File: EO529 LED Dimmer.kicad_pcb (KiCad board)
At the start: 2 copper layers, 76.2 x 45.7 mm, 47 parts, among them J1 VBat, Q1 BC639, Q2 BC639, Q3 BC639, Q4 BC639, U1 NE556, U2 NE556

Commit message: Revision to circuit
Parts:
- removed D10: LED_RGBA, LED_THT:LED_BL-FL7680RGB
- removed D3, D4, D6, D7, D8, D9: 1N4148, Diode_THT:D_DO-35_SOD27_P7.62mm_Horizontal
- removed D5: White, LED_THT:LED_D10.0mm
- added R13: 10k, Resistor_THT:R_Axial_DIN0207_L6.3mm_D2.5mm_P7.62mm_Horizontal, F.Cu at (75.3, 81.7)
- added R14: 10k, Resistor_THT:R_Axial_DIN0207_L6.3mm_D2.5mm_P7.62mm_Horizontal, F.Cu at (82.9, 77.9)
- added R15: 100k, Resistor_THT:R_Axial_DIN0207_L6.3mm_D2.5mm_P7.62mm_Horizontal, F.Cu at (60.7, 38.9)
- added R16: 100k, Resistor_THT:R_Axial_DIN0207_L6.3mm_D2.5mm_P7.62mm_Horizontal, F.Cu at (76.9, 23.3)
- added R17: 1k, Resistor_THT:R_Axial_DIN0207_L6.3mm_D2.5mm_P7.62mm_Horizontal, F.Cu at (66.1, 31.4)
- added R18: 180, Resistor_THT:R_Axial_DIN0207_L6.3mm_D2.5mm_P7.62mm_Horizontal, F.Cu at (47.0, 51.1)
- added R19: 10k, Resistor_THT:R_Axial_DIN0207_L6.3mm_D2.5mm_P7.62mm_Horizontal, F.Cu at (61.3, 81.7)
- added R20: 10k, Resistor_THT:R_Axial_DIN0207_L6.3mm_D2.5mm_P7.62mm_Horizontal, F.Cu at (53.7, 77.9)
- added R21: 100k, Resistor_THT:R_Axial_DIN0207_L6.3mm_D2.5mm_P7.62mm_Horizontal, F.Cu at (39.2, 47.0)
- added R22: 100k, Resistor_THT:R_Axial_DIN0207_L6.3mm_D2.5mm_P7.62mm_Horizontal, F.Cu at (76.9, 19.3)
- added R23: 1k, Resistor_THT:R_Axial_DIN0207_L6.3mm_D2.5mm_P7.62mm_Horizontal, F.Cu at (39.2, 43.0)
- added R24: 220, Resistor_THT:R_Axial_DIN0207_L6.3mm_D2.5mm_P7.62mm_Horizontal, F.Cu at (49.9, 38.9)
- added U3: LM339, Package_DIP:DIP-14_W7.62mm_Socket, F.Cu at (33.4, 87.4)
- D1: value 1N4148 -> White; footprint Diode_THT:D_DO-35_SOD27_P7.62mm_Horizontal -> LED_THT:LED_D10.0mm
- D2: value 1N4148 -> LED_RGBA; footprint Diode_THT:D_DO-35_SOD27_P7.62mm_Horizontal -> LED_THT:LED_BL-FL7680RGB
- R1, R2, R7, R8: value 1k -> 10k
- R10, R3, R4, R9: value 1k -> 100k
- R12: value 1k -> 220
- R5: value 180 -> 1k
- R6: value 10k -> 150
- moved D2 71.5 mm to (88.3, 15.4), turned to 0 degrees
- moved H2 68.9 mm to (87.0, 46.4)
- moved H1 65.7 mm to (87.5, 40.5)
- moved R7 60.0 mm to (75.3, 85.5)
- moved RV2 51.8 mm to (49.3, 102.0), turned to 90 degrees
- moved RV3 48.9 mm to (43.6, 65.2), turned to 270 degrees
- moved C6 48.4 mm to (81.7, 74.0), turned to 90 degrees
- moved R8 47.3 mm to (82.9, 89.3), turned to 180 degrees
- moved Q1 46.7 mm to (80.0, 40.7), turned to 0 degrees
- moved R10 44.7 mm to (66.1, 23.3), turned to 0 degrees
- moved Q4 42.9 mm to (79.5, 46.5), turned to 0 degrees
- moved C3 42.5 mm to (76.6, 93.1), turned to 270 degrees
- moved RV1 39.8 mm to (37.8, 102.0), turned to 90 degrees
- moved C8 39.1 mm to (55.0, 74.0), turned to 90 degrees
- moved R4 37.9 mm to (66.1, 15.2)
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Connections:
- D1 pad 2: Net-(D1-Pad2) -> VCC
- D2 pad 1: Net-(D1-Pad2) -> Red
- D2 pad 2: Net-(D2-Pad2) -> Green
- R1 pad 1: Net-(Q1-Pad3) -> VCC
- R10 pad 1: Net-(Q2-Pad2) -> Net-(R10-Pad1)
- R10 pad 2: Net-(D5-Pad1) -> GND
- R11 pad 1: Net-(Q4-Pad2) -> Net-(Q2-Pad3)
- R11 pad 2: Green -> Net-(R11-Pad2)
- R12 pad 1: Net-(Q3-Pad2) -> Net-(Q2-Pad2)
- R12 pad 2: Blue -> Green
- R2 pad 1: Net-(Q2-Pad3) -> Net-(R1-Pad2)
- R2 pad 2: Net-(R2-Pad2) -> Net-(C2-Pad1)
- R3 pad 2: Net-(D1-Pad2) -> Net-(R3-Pad2)
- R4 pad 1: VCC -> Net-(R4-Pad1)
- R4 pad 2: Net-(D3-Pad2) -> GND
- R5 pad 1: Net-(Q1-Pad2) -> Net-(Q1-Pad3)
- R5 pad 2: Red -> Net-(R5-Pad2)
- R6 pad 1: Net-(Q3-Pad3) -> Net-(Q1-Pad2)
- R6 pad 2: Net-(R6-Pad2) -> Red
- R7 pad 1: Net-(Q4-Pad3) -> VCC
- R8 pad 1: VCC -> Net-(R7-Pad2)
- R8 pad 2: Net-(D6-Pad2) -> Net-(C4-Pad1)
- R9 pad 2: Net-(D8-Pad2) -> Net-(R9-Pad2)
- RV1 pad 1: Net-(D1-Pad1) -> Net-(R4-Pad1)
- RV1 pad 2: Net-(C3-Pad1) -> Net-(RV1-Pad2)
- RV1 pad 3: Net-(D2-Pad2) -> Net-(R3-Pad2)
- RV2 pad 1: Net-(D3-Pad1) -> Net-(R10-Pad1)
- RV2 pad 2: Net-(C4-Pad1) -> Net-(RV2-Pad2)
- RV2 pad 3: Net-(D4-Pad2) -> Net-(R9-Pad2)
- RV3 pad 2: Net-(C7-Pad1) -> Net-(RV3-Pad2)
- RV4 pad 2: Net-(C8-Pad1) -> Net-(RV4-Pad2)
- U1 pad 1: Net-(D1-Pad2) -> Net-(R1-Pad2)
- U1 pad 11: Net-(C2-Pad1) -> Net-(C3-Pad1)
- U1 pad 13: Net-(D3-Pad2) -> Net-(R7-Pad2)
- U1 pad 2: Net-(C3-Pad1) -> Net-(C2-Pad1)
- U1 pad 5: Net-(R1-Pad2) -> (no net)
- U1 pad 6: Net-(C3-Pad1) -> Net-(C2-Pad1)
- U1 pad 9: Net-(R2-Pad2) -> (no net)
- U2 pad 1: Net-(D6-Pad2) -> Net-(R13-Pad2)
- U2 pad 11: Net-(C6-Pad1) -> Net-(C7-Pad1)
- U2 pad 13: Net-(D8-Pad2) -> Net-(R19-Pad2)
- U2 pad 2: Net-(C7-Pad1) -> Net-(C6-Pad1)
- U2 pad 5: Net-(R6-Pad2) -> (no net)
- U2 pad 6: Net-(C7-Pad1) -> Net-(C6-Pad1)
- U2 pad 9: Net-(R7-Pad2) -> (no net)
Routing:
- net GND: track 210.0 -> 61.6 mm
- net Net-(C6-Pad1): track 3.91 -> 76.7 mm
- net Green: track 70.3 -> 0.00 mm
- net Red: track 65.9 -> 0.00 mm
- net VCC: track 119.5 -> 59.6 mm
- net Blue: track 44.4 -> 0.00 mm
- net Net-(C4-Pad1): track 39.2 -> 80.8 mm
- net Net-(C2-Pad1): track 3.91 -> 41.9 mm
- net Net-(C7-Pad1): track 40.2 -> 4.45 mm
- net Net-(C3-Pad1): track 37.2 -> 4.45 mm
- net Net-(D5-Pad1): track 32.6 -> 0.00 mm
- net Net-(D6-Pad2): track 24.0 -> 0.00 mm
- net Net-(D1-Pad2): track 23.6 -> 0.00 mm
- net Net-(D3-Pad2): track 23.2 -> 0.00 mm
- net Net-(D8-Pad2): track 22.6 -> 0.00 mm
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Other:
- board outline removed
- board text removed: "+ -"
- board text removed: "PWM LED Controller Board EO529 Part A"
- board text removed: "University of Brighton EEE V1.0 Aria Tso 21839447"

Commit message: Fixed broken files
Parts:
- added U4: LM393, Package_DIP:DIP-8_W7.62mm_Socket, F.Cu at (129.5, 90.8)
- R24: value 220 -> 150
- R6: value 150 -> 220
- U3: value LM339 -> LM393; footprint Package_DIP:DIP-14_W7.62mm_Socket -> Package_DIP:DIP-8_W7.62mm_Socket
- moved D1 109.1 mm to (110.5, 116.8), turned to 90 degrees
- moved R16 106.2 mm to (128.3, 116.2)
- moved R18 103.3 mm to (137.2, 101.6), turned to 270 degrees
- moved R11 102.2 mm to (133.3, 87.6), turned to 90 degrees
- moved R15 101.0 mm to (125.7, 116.2), turned to 180 degrees
- moved D2 100.0 mm to (97.8, 114.9)
- moved R12 98.0 mm to (137.2, 87.6), turned to 90 degrees
- moved R17 97.2 mm to (133.3, 101.6), turned to 270 degrees
- moved RV3 96.9 mm to (128.2, 112.2), turned to 90 degrees
- moved R22 92.5 mm to (73.7, 111.8), turned to 270 degrees
- moved H4 89.7 mm to (139.7, 119.4)
- moved R21 84.7 mm to (95.9, 109.9), turned to 180 degrees
- moved Q3 80.3 mm to (137.2, 97.2), turned to 180 degrees
- moved J1 78.3 mm to (88.9, 118.1), turned to 180 degrees
- moved RV2 78.1 mm to (123.2, 77.0), turned to 270 degrees
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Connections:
- R12 pad 2: Green -> Blue
- R24 pad 2: Blue -> Red
- R6 pad 2: Red -> Green
- U1 pad 5: (no net) -> Net-(U1-Pad5)
- U1 pad 9: (no net) -> Net-(U1-Pad9)
- U2 pad 5: (no net) -> Net-(U2-Pad5)
- U2 pad 9: (no net) -> Net-(U2-Pad9)
- U3 pad 1: Net-(R11-Pad2) -> Net-(R23-Pad2)
- U3 pad 2: Net-(R5-Pad2) -> Net-(C8-Pad1)
- U3 pad 3: VCC -> Net-(RV4-Pad2)
- U3 pad 4: Net-(C2-Pad1) -> GND
- U3 pad 6: Net-(C4-Pad1) -> Net-(C2-Pad1)
- U3 pad 7: Net-(RV2-Pad2) -> Net-(R5-Pad2)
- U3 pad 8: Net-(C6-Pad1) -> VCC
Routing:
- net GND: track 61.6 -> 285.7 mm
- net VCC: track 59.6 -> 194.7 mm
- net Blue: track 0.00 -> 75.9 mm
- net Green: track 0.00 -> 70.1 mm
- net Net-(C6-Pad1): track 76.7 -> 31.2 mm
- net Net-(C4-Pad1): track 80.8 -> 44.0 mm
- net Net-(D1-Pad1): track 0.00 -> 31.3 mm
- net Red: track 0.00 -> 27.5 mm
- net Net-(R17-Pad2): track 0.00 -> 17.6 mm
- net Net-(R23-Pad2): track 0.00 -> 14.0 mm
- net Net-(Q1-Pad3): track 0.00 -> 13.4 mm
- net Net-(R11-Pad2): track 0.00 -> 12.4 mm
- net Net-(Q2-Pad3): track 0.00 -> 12.2 mm
- net Net-(R22-Pad1): track 0.00 -> 12.0 mm
- net Net-(R9-Pad2): track 0.00 -> 11.7 mm
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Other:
- board outline added: 77.5 x 52.7 mm
- board text added: "- +"

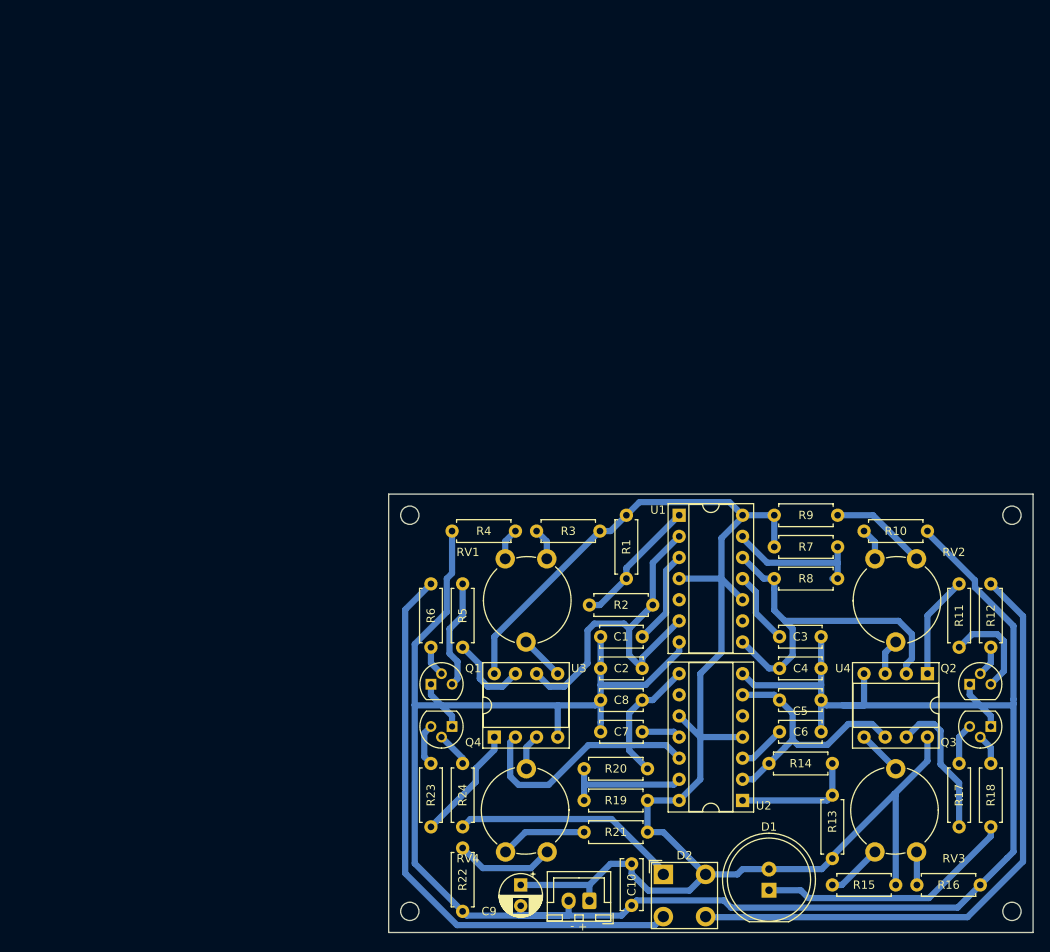
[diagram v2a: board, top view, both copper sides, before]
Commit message: Revert "Fixed broken files"
This reverts commit e50aa6ede737ee02b3ead64743985b0a59545fc6.
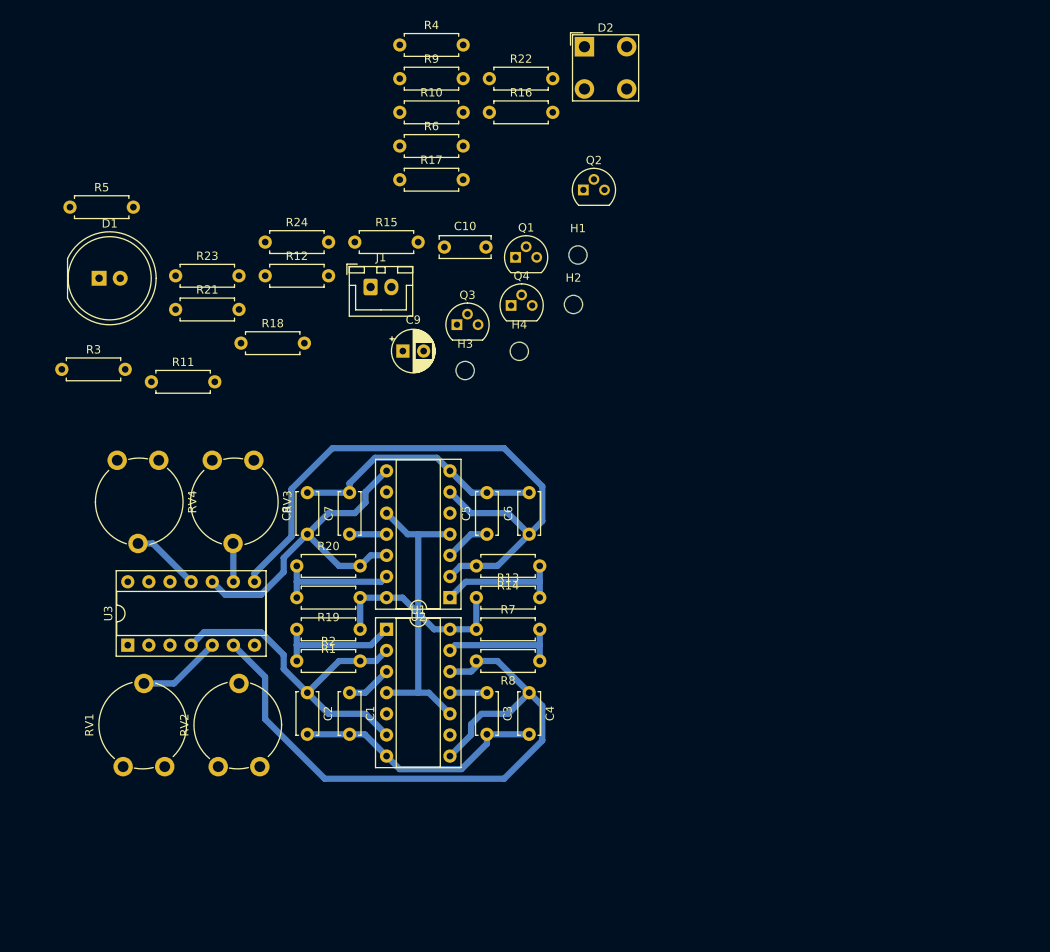
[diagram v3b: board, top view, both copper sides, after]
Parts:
- removed U4: LM393, Package_DIP:DIP-8_W7.62mm_Socket
- R24: value 150 -> 220
- R6: value 220 -> 150
- U3: value LM393 -> LM339; footprint Package_DIP:DIP-8_W7.62mm_Socket -> Package_DIP:DIP-14_W7.62mm_Socket
- moved D1 109.1 mm to (30.0, 43.3), turned to 0 degrees
- moved R16 106.2 mm to (76.9, 23.3)
- moved R18 103.3 mm to (47.0, 51.1), turned to 0 degrees
- moved R11 102.2 mm to (36.2, 55.7), turned to 0 degrees
- moved R15 101.0 mm to (60.7, 38.9), turned to 0 degrees
- moved D2 100.0 mm to (88.3, 15.4)
- moved R12 98.0 mm to (49.9, 43.0), turned to 0 degrees
- moved R17 97.2 mm to (66.1, 31.4), turned to 0 degrees
- moved RV3 96.9 mm to (43.6, 65.2), turned to 270 degrees
- moved R22 92.5 mm to (76.9, 19.3), turned to 0 degrees
- moved H4 89.7 mm to (80.5, 52.0)
- moved R21 84.7 mm to (39.2, 47.0), turned to 0 degrees
- moved Q3 80.3 mm to (73.0, 48.8), turned to 0 degrees
- moved J1 78.3 mm to (62.6, 44.3), turned to 0 degrees
- moved RV2 78.1 mm to (49.3, 102.0), turned to 90 degrees
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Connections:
- R12 pad 2: Blue -> Green
- R24 pad 2: Red -> Blue
- R6 pad 2: Green -> Red
- U1 pad 5: Net-(U1-Pad5) -> (no net)
- U1 pad 9: Net-(U1-Pad9) -> (no net)
- U2 pad 5: Net-(U2-Pad5) -> (no net)
- U2 pad 9: Net-(U2-Pad9) -> (no net)
- U3 pad 1: Net-(R23-Pad2) -> Net-(R11-Pad2)
- U3 pad 2: Net-(C8-Pad1) -> Net-(R5-Pad2)
- U3 pad 3: Net-(RV4-Pad2) -> VCC
- U3 pad 4: GND -> Net-(C2-Pad1)
- U3 pad 6: Net-(C2-Pad1) -> Net-(C4-Pad1)
- U3 pad 7: Net-(R5-Pad2) -> Net-(RV2-Pad2)
- U3 pad 8: VCC -> Net-(C6-Pad1)
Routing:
- net GND: track 285.7 -> 61.6 mm
- net VCC: track 194.7 -> 59.6 mm
- net Blue: track 75.9 -> 0.00 mm
- net Green: track 70.1 -> 0.00 mm
- net Net-(C6-Pad1): track 31.2 -> 76.7 mm
- net Net-(C4-Pad1): track 44.0 -> 80.8 mm
- net Net-(D1-Pad1): track 31.3 -> 0.00 mm
- net Red: track 27.5 -> 0.00 mm
- net Net-(R17-Pad2): track 17.6 -> 0.00 mm
- net Net-(R23-Pad2): track 14.0 -> 0.00 mm
- net Net-(Q1-Pad3): track 13.4 -> 0.00 mm
- net Net-(R11-Pad2): track 12.4 -> 0.00 mm
- net Net-(Q2-Pad3): track 12.2 -> 0.00 mm
- net Net-(R22-Pad1): track 12.0 -> 0.00 mm
- net Net-(R9-Pad2): track 11.7 -> 0.00 mm
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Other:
- board outline removed
- board text removed: "- +"
